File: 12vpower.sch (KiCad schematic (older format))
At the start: 17 parts, among them J1 Conn_02x08_Odd_Even, P1 15 in, P2 12, P3 12, U1 L7812, U2 L7912, U3 L7805

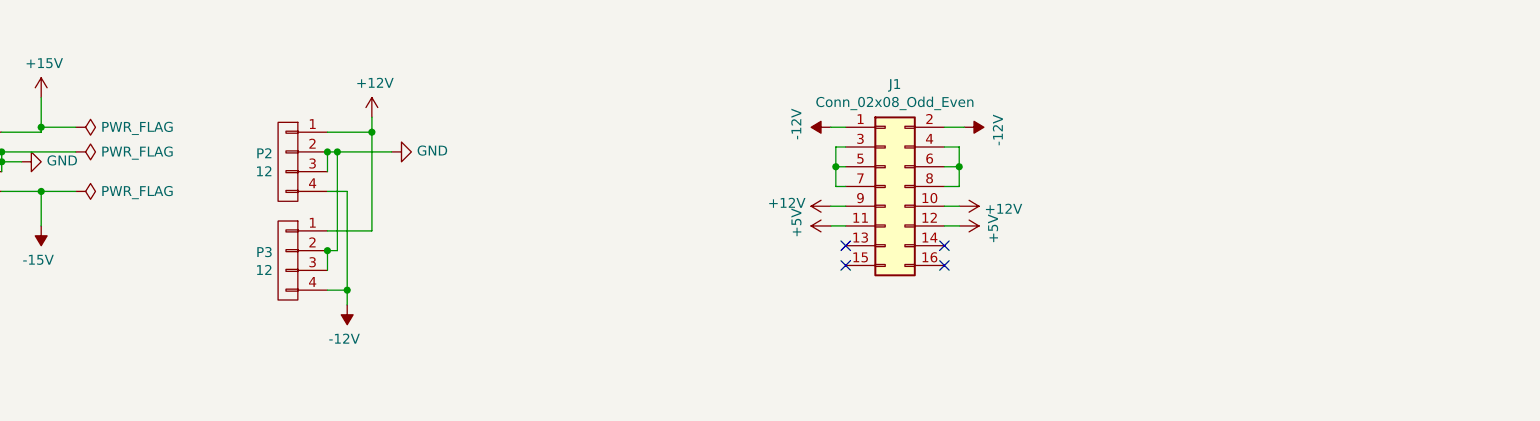
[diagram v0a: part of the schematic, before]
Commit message: labels and more euro power
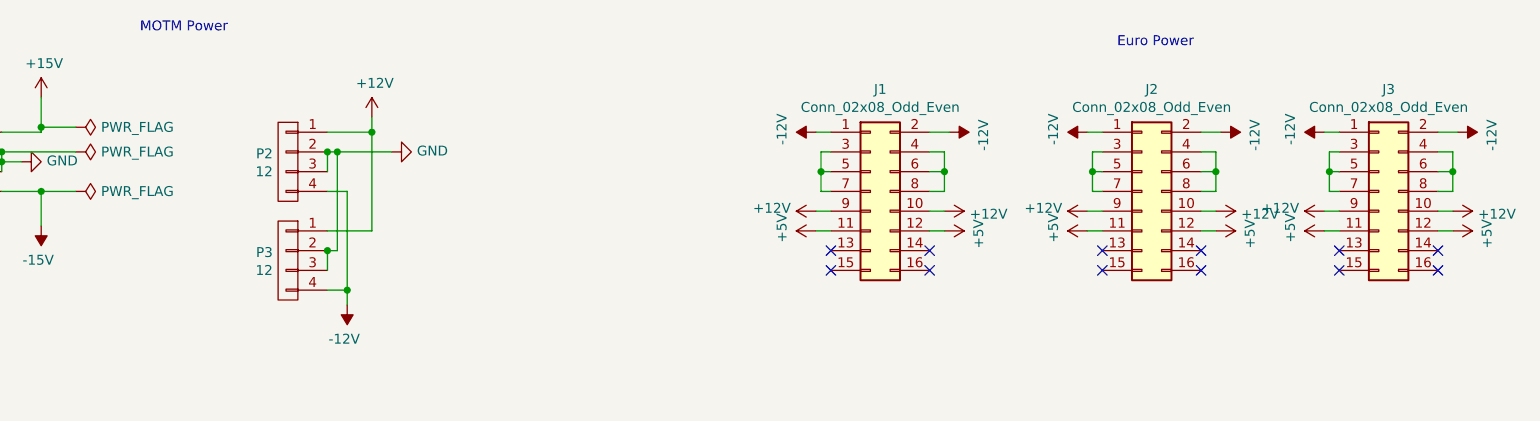
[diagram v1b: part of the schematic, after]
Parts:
- added J1, J3: Conn_02x08_Odd_Even, symbol Connector_Generic:Conn_02x08_Odd_Even
- renumbered J1 to J2
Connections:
- net +12V: now also J1.10 (Pin_10), J1.9 (Pin_9), J3.10 (Pin_10), J3.9 (Pin_9)
- net +5V: now also J1.11 (Pin_11), J1.12 (Pin_12), J3.11 (Pin_11), J3.12 (Pin_12)
- net -12V: now also J1.1 (Pin_1), J1.2 (Pin_2), J3.1 (Pin_1), J3.2 (Pin_2)
- new net: J1.3 (Pin_3), J1.5 (Pin_5), J1.7 (Pin_7)
- new net: J1.4 (Pin_4), J1.6 (Pin_6), J1.8 (Pin_8)
- new net: J3.3 (Pin_3), J3.5 (Pin_5), J3.7 (Pin_7)
- new net: J3.4 (Pin_4), J3.6 (Pin_6), J3.8 (Pin_8)
- no-connect marks 4 -> 12
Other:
- note added: "Euro Power"
- note added: "MOTM Power"
- moved on the sheet: J2

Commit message: footprints
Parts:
- C1, C2, C5, C6, C9: footprint (none) -> Capacitor_THT:CP_Radial_D7.5mm_P2.50mm
- C10, C3, C4, C7, C8: footprint (none) -> Capacitor_THT:C_Disc_D4.3mm_W1.9mm_P5.00mm
- J1, J2, J3: footprint (none) -> Connector_PinHeader_2.54mm:PinHeader_2x08_P2.54mm_Vertical
- P1, P2, P3: footprint (none) -> mta-156:MTA-156-4
- U1, U2, U3: footprint (none) -> Package_TO_SOT_THT:TO-220-3_Vertical
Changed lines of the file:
@@
 F 0 "P1" H 1302 1316 50  0000 L CNN
 F 1 "15 in" H 1302 1225 50  0000 L CNN
-F 2 "" H 1225 1275 50  0000 C CNN
+F 2 "mta-156:MTA-156-4" H 1225 1275 50  0001 C CNN
 F 3 "" H 1225 1275 50  0000 C CNN
 	1    1225 1275
@@
 F 0 "P2" H 2952 1316 50  0000 L CNN
 F 1 "12" H 2952 1225 50  0000 L CNN
-F 2 "" H 2875 1275 50  0000 C CNN
+F 2 "mta-156:MTA-156-4" H 2875 1275 50  0001 C CNN
 F 3 "" H 2875 1275 50  0000 C CNN
 	1    2875 1275
@@
 F 0 "P3" H 2952 1816 50  0000 L CNN
 F 1 "12" H 2952 1725 50  0000 L CNN
-F 2 "" H 2875 1775 50  0000 C CNN
+F 2 "mta-156:MTA-156-4" H 2875 1775 50  0001 C CNN
 F 3 "" H 2875 1775 50  0000 C CNN
 	1    2875 1775
@@
 F 0 "U1" H 2200 4592 50  0000 C CNN
 F 1 "L7812" H 2200 4501 50  0000 C CNN
-F 2 "" H 2225 4200 50  0001 L CIN
+F 2 "Package_TO_SOT_THT:TO-220-3_Vertical" H 2225 4200 50  0001 L CIN
 F 3 "http://www.st.com/content/ccc/resource/technical/document/datasheet/41/4f/b3/b0/12/d4/47/88/CD00000444.pdf/files/CD00000444.pdf/jcr:content/translations/en.CD00000444.pdf" H 2200 4300 50  0001 C CNN
 	1    2200 4350
@@
 F 0 "U2" H 2200 5425 50  0000 C CNN
 F 1 "L7912" H 2200 5334 50  0000 C CNN
-F 2 "" H 2200 5375 50  0001 C CIN
+F 2 "Package_TO_SOT_THT:TO-220-3_Vertical" H 2200 5375 50  0001 C CIN
 F 3 "http://www.st.com/content/ccc/resource/technical/document/datasheet/c9/16/86/41/c7/2b/45/f2/CD00000450.pdf/files/CD00000450.pdf/jcr:content/translations/en.CD00000450.pdf" H 2200 5575 50  0001 C CNN
 	1    2200 5575
@@
 F 0 "U3" H 3950 4592 50  0000 C CNN
 F 1 "L7805" H 3950 4501 50  0000 C CNN
-F 2 "" H 3975 4200 50  0001 L CIN
+F 2 "Package_TO_SOT_THT:TO-220-3_Vertical" H 3975 4200 50  0001 L CIN
 F 3 "http://www.st.com/content/ccc/resource/technical/document/datasheet/41/4f/b3/b0/12/d4/47/88/CD00000444.pdf/files/CD00000444.pdf/jcr:content/translations/en.CD00000444.pdf" H 3950 4300 50  0001 C CNN
 	1    3950 4350
@@
 F 0 "C1" H 1543 4746 50  0000 L CNN
 F 1 "CP" H 1543 4655 50  0000 L CNN
-F 2 "" H 1463 4550 50  0001 C CNN
+F 2 "Capacitor_THT:CP_Radial_D7.5mm_P2.50mm" H 1463 4550 50  0001 C CNN
 F 3 "~" H 1425 4700 50  0001 C CNN
 	1    1425 4700
@@
 F 0 "C2" H 1543 5296 50  0000 L CNN
 F 1 "CP" H 1543 5205 50  0000 L CNN
-F 2 "" H 1463 5100 50  0001 C CNN
+F 2 "Capacitor_THT:CP_Radial_D7.5mm_P2.50mm" H 1463 5100 50  0001 C CNN
 F 3 "~" H 1425 5250 50  0001 C CNN
 	1    1425 5250
@@
 F 0 "C5" H 2743 4746 50  0000 L CNN
 F 1 "CP" H 2743 4655 50  0000 L CNN
-F 2 "" H 2663 4550 50  0001 C CNN
+F 2 "Capacitor_THT:CP_Radial_D7.5mm_P2.50mm" H 2663 4550 50  0001 C CNN
 F 3 "~" H 2625 4700 50  0001 C CNN
 	1    2625 4700
@@
 F 0 "C6" H 2743 5296 50  0000 L CNN
 F 1 "CP" H 2743 5205 50  0000 L CNN
-F 2 "" H 2663 5100 50  0001 C CNN
+F 2 "Capacitor_THT:CP_Radial_D7.5mm_P2.50mm" H 2663 5100 50  0001 C CNN
 F 3 "~" H 2625 5250 50  0001 C CNN
 	1    2625 5250
@@
 F 0 "C9" H 4568 4746 50  0000 L CNN
 F 1 "CP" H 4568 4655 50  0000 L CNN
-F 2 "" H 4488 4550 50  0001 C CNN
+F 2 "Capacitor_THT:CP_Radial_D7.5mm_P2.50mm" H 4488 4550 50  0001 C CNN
 F 3 "~" H 4450 4700 50  0001 C CNN
 	1    4450 4700
@@
 F 0 "C3" H 1915 4746 50  0000 L CNN
 F 1 "C" H 1915 4655 50  0000 L CNN
-F 2 "" H 1838 4550 50  0001 C CNN
+F 2 "Capacitor_THT:C_Disc_D4.3mm_W1.9mm_P5.00mm" H 1838 4550 50  0001 C CNN
 F 3 "~" H 1800 4700 50  0001 C CNN
 	1    1800 4700
@@
 F 0 "C4" H 1915 5296 50  0000 L CNN
 F 1 "C" H 1915 5205 50  0000 L CNN
-F 2 "" H 1838 5100 50  0001 C CNN
+F 2 "Capacitor_THT:C_Disc_D4.3mm_W1.9mm_P5.00mm" H 1838 5100 50  0001 C CNN
 F 3 "~" H 1800 5250 50  0001 C CNN
 	1    1800 5250
@@
 F 0 "C7" H 3265 4746 50  0000 L CNN
 F 1 "C" H 3265 4655 50  0000 L CNN
-F 2 "" H 3188 4550 50  0001 C CNN
+F 2 "Capacitor_THT:C_Disc_D4.3mm_W1.9mm_P5.00mm" H 3188 4550 50  0001 C CNN
 F 3 "~" H 3150 4700 50  0001 C CNN
 	1    3150 4700
@@
 F 0 "C8" H 3265 5296 50  0000 L CNN
 F 1 "C" H 3265 5205 50  0000 L CNN
-F 2 "" H 3188 5100 50  0001 C CNN
+F 2 "Capacitor_THT:C_Disc_D4.3mm_W1.9mm_P5.00mm" H 3188 5100 50  0001 C CNN
 F 3 "~" H 3150 5250 50  0001 C CNN
 	1    3150 5250
@@
 F 0 "C10" H 4890 4746 50  0000 L CNN
 F 1 "C" H 4890 4655 50  0000 L CNN
-F 2 "" H 4813 4550 50  0001 C CNN
+F 2 "Capacitor_THT:C_Disc_D4.3mm_W1.9mm_P5.00mm" H 4813 4550 50  0001 C CNN
 F 3 "~" H 4775 4700 50  0001 C CNN
 	1    4775 4700
@@
 F 0 "J2" H 7250 1942 50  0000 C CNN
 F 1 "Conn_02x08_Odd_Even" H 7250 1851 50  0000 C CNN
-F 2 "" H 7200 1425 50  0001 C CNN
+F 2 "Connector_PinHeader_2.54mm:PinHeader_2x08_P2.54mm_Vertical" H 7200 1425 50  0001 C CNN
 F 3 "~" H 7200 1425 50  0001 C CNN
 	1    7200 1425
@@
 F 0 "J1" H 5875 1942 50  0000 C CNN
 F 1 "Conn_02x08_Odd_Even" H 5875 1851 50  0000 C CNN
-F 2 "" H 5825 1425 50  0001 C CNN
+F 2 "Connector_PinHeader_2.54mm:PinHeader_2x08_P2.54mm_Vertical" H 5825 1425 50  0001 C CNN
 F 3 "~" H 5825 1425 50  0001 C CNN
 	1    5825 1425
@@
 F 0 "J3" H 8450 1942 50  0000 C CNN
 F 1 "Conn_02x08_Odd_Even" H 8450 1851 50  0000 C CNN
-F 2 "" H 8400 1425 50  0001 C CNN
+F 2 "Connector_PinHeader_2.54mm:PinHeader_2x08_P2.54mm_Vertical" H 8400 1425 50  0001 C CNN
 F 3 "~" H 8400 1425 50  0001 C CNN
 	1    8400 1425

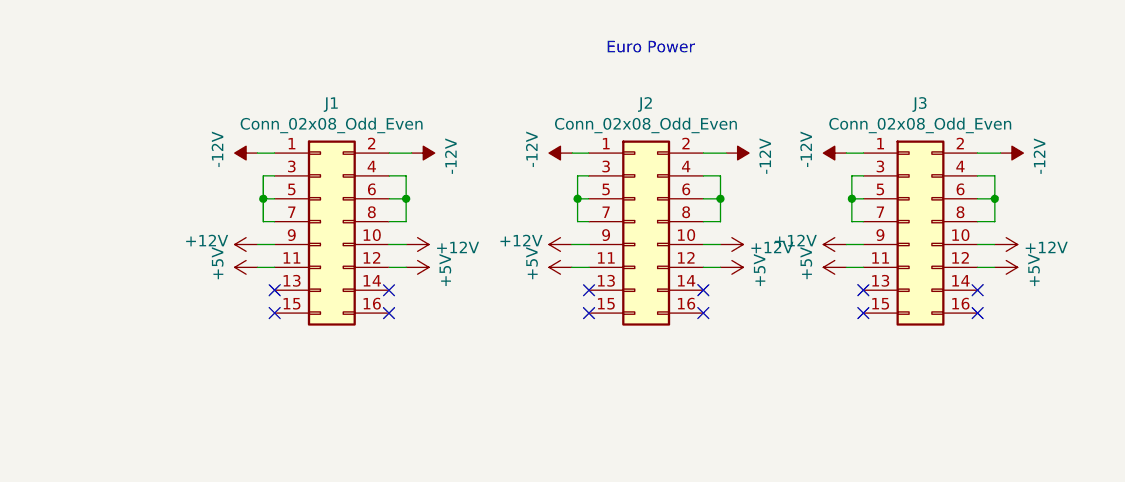
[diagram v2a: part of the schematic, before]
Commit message: forgot euro ground
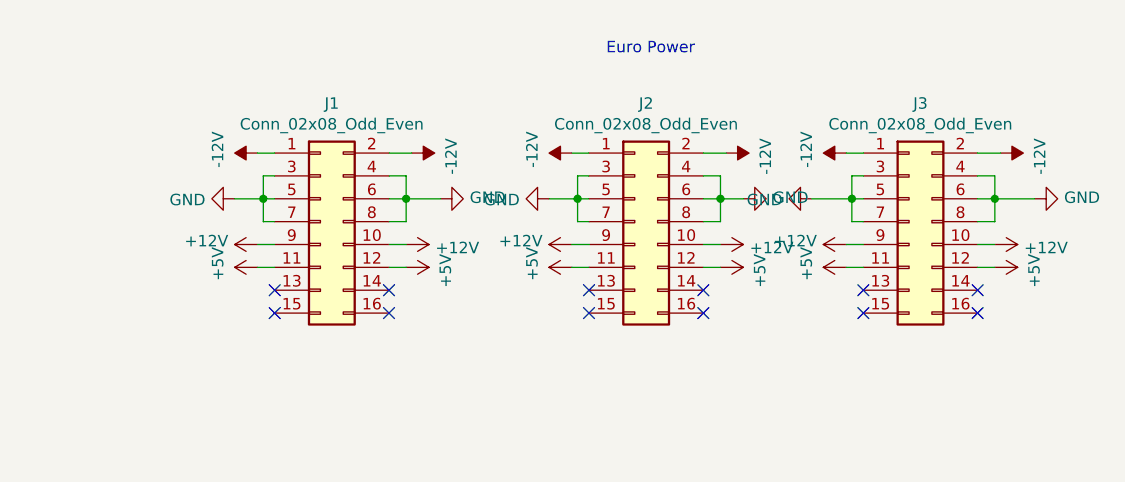
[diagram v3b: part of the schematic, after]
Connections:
- net GND: now also J1.3 (Pin_3), J1.4 (Pin_4), J1.5 (Pin_5), J1.6 (Pin_6), J1.7 (Pin_7), J1.8 (Pin_8), J2.3 (Pin_3), J2.4 (Pin_4), J2.5 (Pin_5), J2.6 (Pin_6), J2.7 (Pin_7), J2.8 (Pin_8), J3.3 (Pin_3), J3.4 (Pin_4), J3.5 (Pin_5), J3.6 (Pin_6), J3.7 (Pin_7), J3.8 (Pin_8)
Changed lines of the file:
@@
 Text Notes 2125 625  0    50   ~ 0
 MOTM Power
+$Comp
+L power:GND #PWR?
+U 1 1 5C8EAD12
+P 5450 1325
+F 0 "#PWR?" H 5450 1075 50  0001 C CNN
+F 1 "GND" V 5455 1197 50  0000 R CNN
+F 2 "" H 5450 1325 50  0001 C CNN
+F 3 "" H 5450 1325 50  0001 C CNN
+	1    5450 1325
+	0    1    1    0
+$EndComp
+$Comp
+L power:GND #PWR?
+U 1 1 5C8EAD69
+P 6350 1325
+F 0 "#PWR?" H 6350 1075 50  0001 C CNN
+F 1 "GND" V 6355 1197 50  0000 R CNN
+F 2 "" H 6350 1325 50  0001 C CNN
+F 3 "" H 6350 1325 50  0001 C CNN
+	1    6350 1325
+	0    -1   -1   0
+$EndComp
+Wire Wire Line
+	5450 1325 5575 1325
+Wire Wire Line
+	6200 1325 6350 1325
+$Comp
+L power:GND #PWR?
+U 1 1 5C8F2235
+P 6825 1325
+F 0 "#PWR?" H 6825 1075 50  0001 C CNN
+F 1 "GND" V 6830 1197 50  0000 R CNN
+F 2 "" H 6825 1325 50  0001 C CNN
+F 3 "" H 6825 1325 50  0001 C CNN
+	1    6825 1325
+	0    1    1    0
+$EndComp
+Wire Wire Line
+	6825 1325 6950 1325
+$Comp
+L power:GND #PWR?
+U 1 1 5C8F5E5F
+P 7675 1325
+F 0 "#PWR?" H 7675 1075 50  0001 C CNN
+F 1 "GND" V 7680 1197 50  0000 R CNN
+F 2 "" H 7675 1325 50  0001 C CNN
+F 3 "" H 7675 1325 50  0001 C CNN
+	1    7675 1325
+	0    -1   -1   0
+$EndComp
+Wire Wire Line
+	7675 1325 7575 1325
+$Comp
+L power:GND #PWR?
+U 1 1 5C8F9BD4
+P 7975 1325
+F 0 "#PWR?" H 7975 1075 50  0001 C CNN
+F 1 "GND" V 7980 1197 50  0000 R CNN
+F 2 "" H 7975 1325 50  0001 C CNN
+F 3 "" H 7975 1325 50  0001 C CNN
+	1    7975 1325
+	0    1    1    0
+$EndComp
+Wire Wire Line
+	7975 1325 8150 1325
+$Comp
+L power:GND #PWR?
+U 1 1 5C8FD9FC
+P 8950 1325
+F 0 "#PWR?" H 8950 1075 50  0001 C CNN
+F 1 "GND" V 8955 1197 50  0000 R CNN
+F 2 "" H 8950 1325 50  0001 C CNN
+F 3 "" H 8950 1325 50  0001 C CNN
+	1    8950 1325
+	0    -1   -1   0
+$EndComp
+Wire Wire Line
+	8950 1325 8775 1325
 $EndSCHEMATC
